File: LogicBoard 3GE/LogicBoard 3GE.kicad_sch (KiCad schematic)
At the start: 163 parts, among them IC201 2363, IC202 74LS00, IC203 74LS32, IC204 2114, IC205 2114, IC206 68A09, IC207 6522, IC208 AY3-8912, IC301 MC1408, IC302 CD4052B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

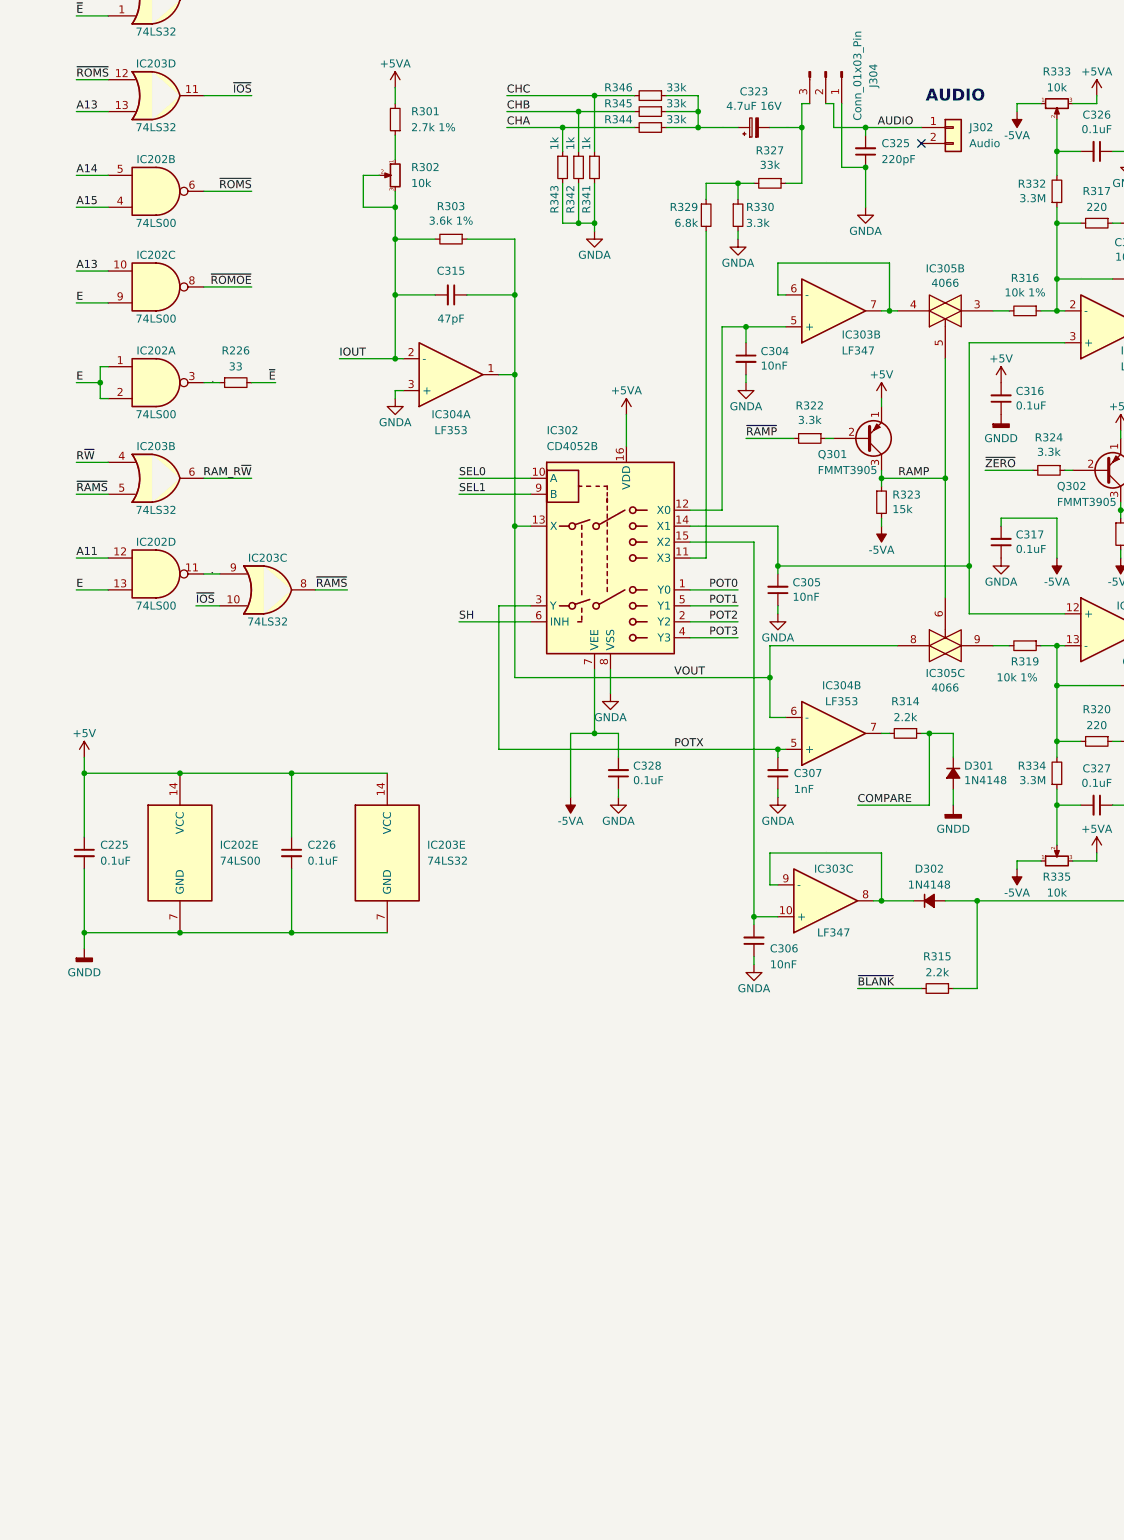
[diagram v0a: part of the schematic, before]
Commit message: added lm386 audio circuit
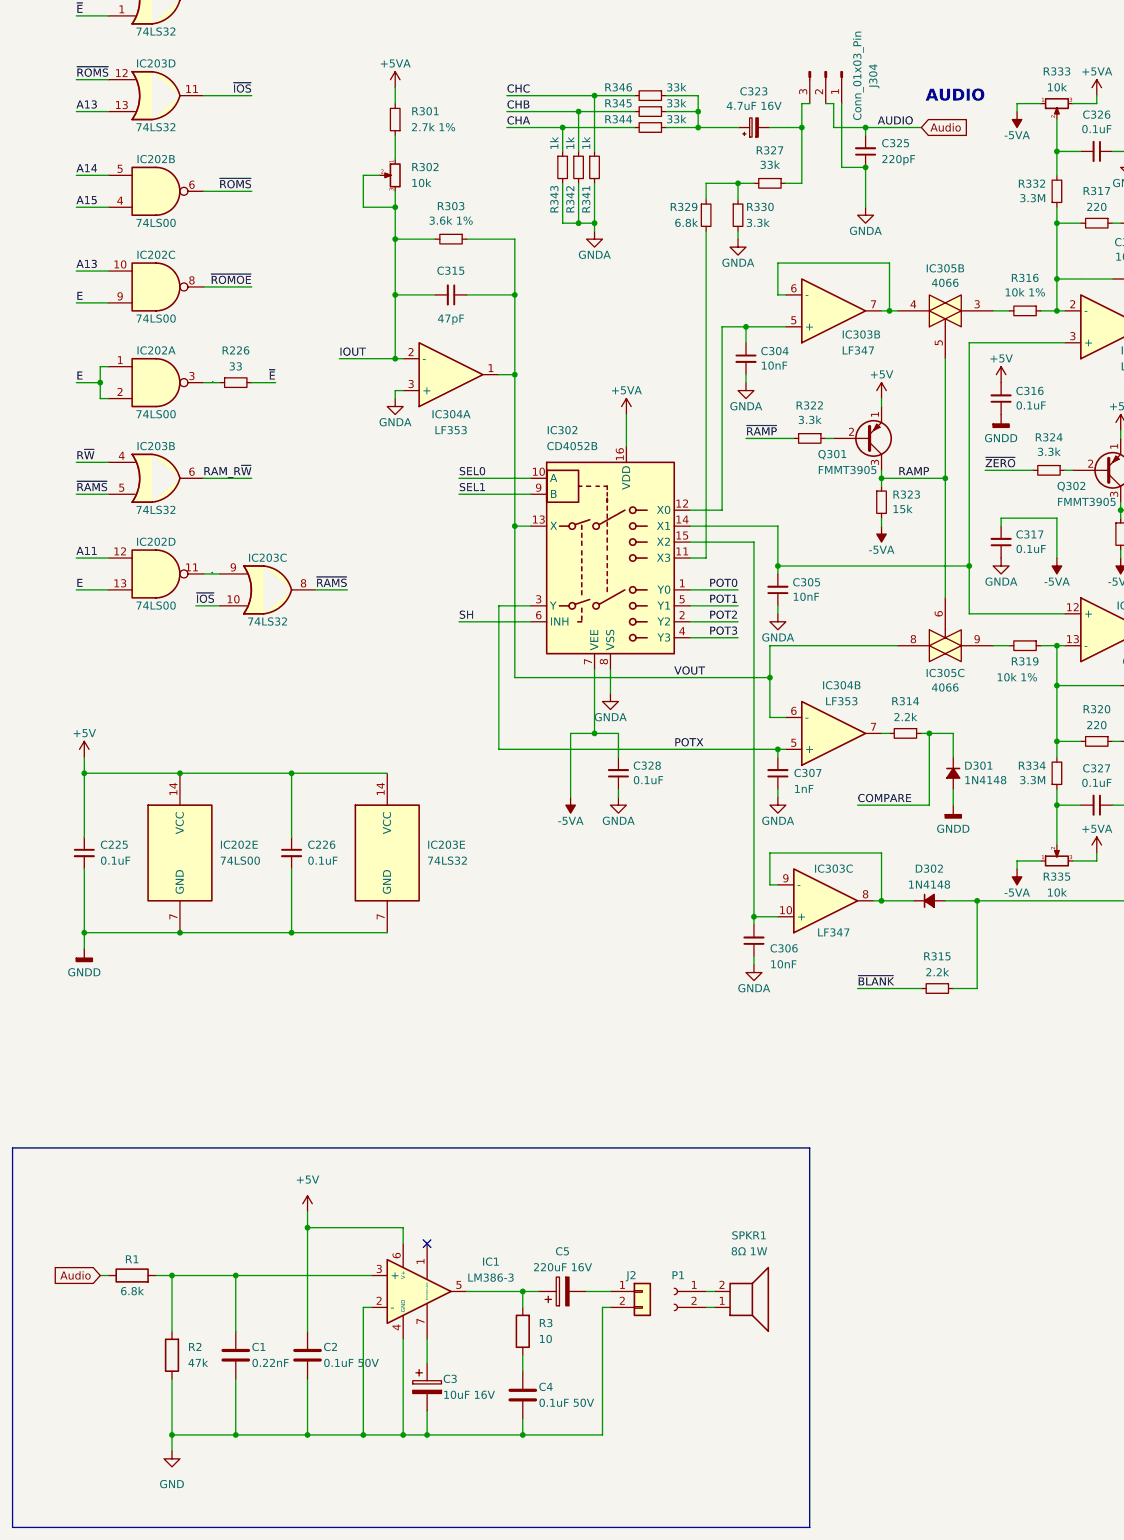
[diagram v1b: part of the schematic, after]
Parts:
- removed J302: Audio, Connector_Molex:Molex_KK-254_AE-6410-02A_1x02_P2.54mm_Vertical, symbol Connector_Generic:Conn_01x02
- added C1: 0.22nF, symbol Device:C
- added C2, C4: 0.1uF 50V, symbol Device:C
- added C3: 10uF 16V, symbol Device:C_Polarized
- added C5: 220uF 16V, symbol Device:C_Polarized
- added IC1: LM386-3, symbol Vectrex:LM386-3
- added J2: Conn_01x02, symbol Connector_Generic:Conn_01x02
- added P1: Conn_01x02_Female, symbol Connector:Conn_01x02_Female
- added R1: 6.8k, symbol Device:R
- added R2: 47k, symbol Device:R
- added R3: 10, symbol Device:R
- added SPKR1: 8Ω 1W, symbol Device:Speaker
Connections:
- net +5V: now also C2.2, IC1.6 (V+)
- net GND: now also C1.2, C2.1, C3.2, C4.2, IC1.2 (-), IC1.4 (GND), J2.2 (Pin_2), R2.1
- net AUDIO renamed Audio
- net Audio: now also R1.1
- new net: P1.2 (Pin_2), SPKR1.1
- new net: P1.1 (Pin_1), SPKR1.2
- new net: C4.1, R3.1
- new net: C5.1, IC1.5, R3.2
- new net: C1.1, IC1.3 (+), R1.2, R2.2
- new net: C3.1, IC1.7 (BYPASS)
- new net: C5.2, J2.1 (Pin_1)

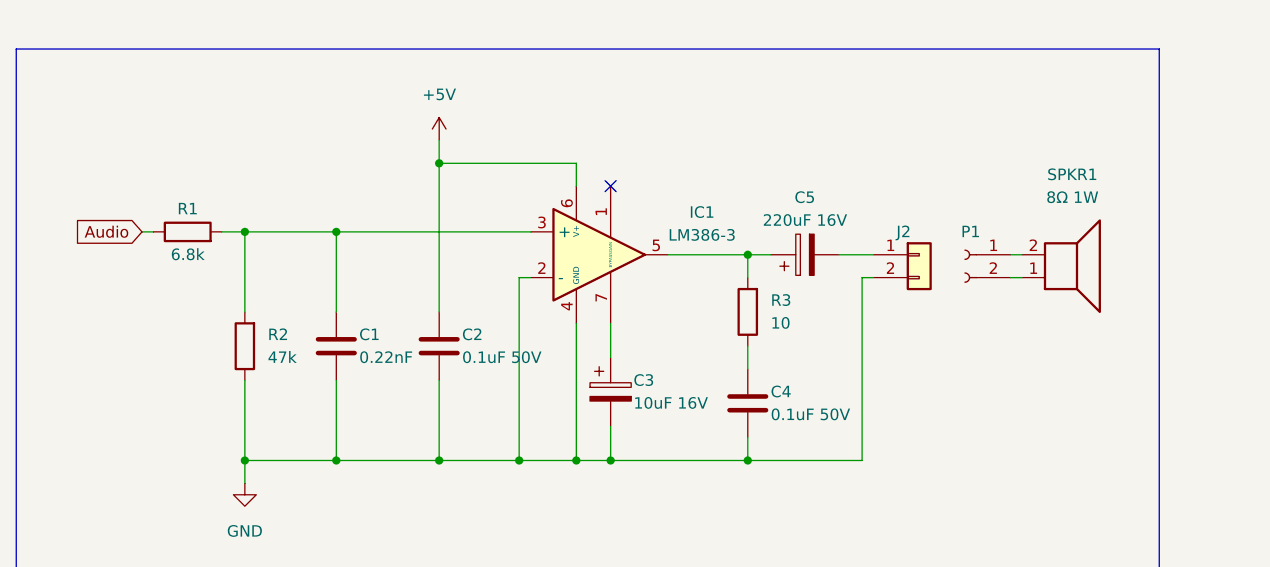
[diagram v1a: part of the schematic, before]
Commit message: added lm386 again, Added MD_90SM footprint. Solve all DRC Conflicts
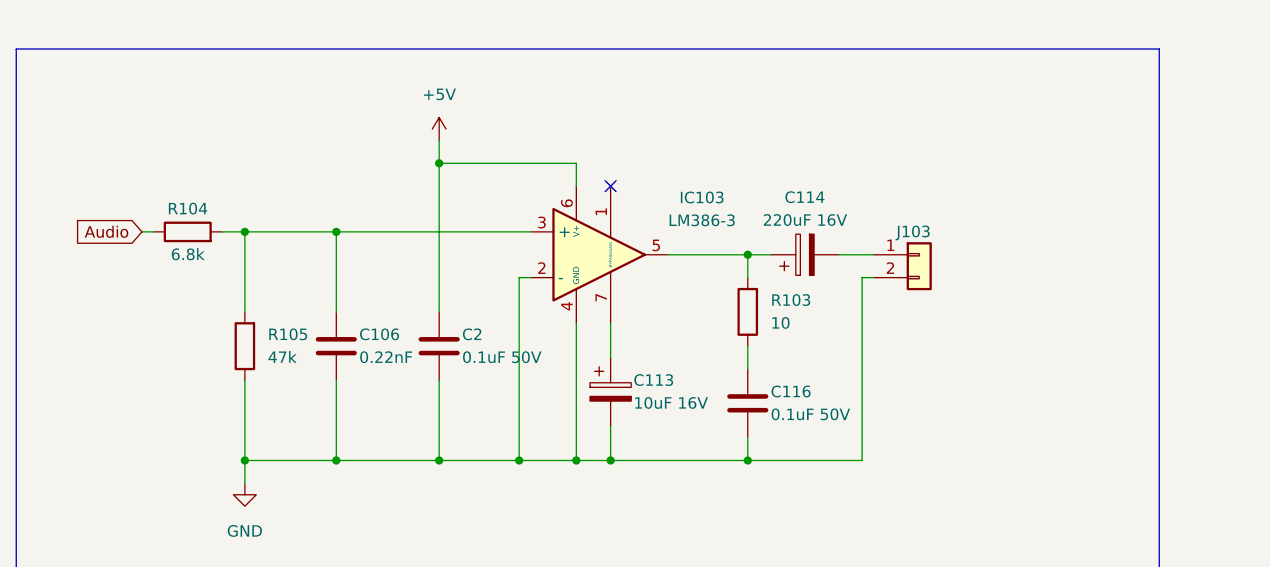
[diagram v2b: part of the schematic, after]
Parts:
- removed P1: Conn_01x02_Female, symbol Connector:Conn_01x02_Female
- removed SPKR1: 8Ω 1W, symbol Device:Speaker
- C106: renamed from C1; footprint (none) -> Capacitor_SMD:C_0805_2012Metric
- C113: renamed from C3; footprint (none) -> Capacitor_SMD:CP_Elec_4x5.3
- C114: renamed from C5; footprint (none) -> Capacitor_SMD:CP_Elec_8x10.5
- C116: renamed from C4; footprint (none) -> Capacitor_SMD:C_0805_2012Metric
- C2: footprint (none) -> Capacitor_SMD:C_0805_2012Metric
- IC103: renamed from IC1; footprint (none) -> Package_SO:SOIC-8-1EP_3.9x4.9mm_P1.27mm_EP2.29x3mm
- J103: renamed from J2; footprint (none) -> Connector_JST:JST_EH_B2B-EH-A_1x02_P2.50mm_Vertical
- R103: renamed from R3; footprint (none) -> Resistor_SMD:R_0805_2012Metric
- R104: renamed from R1; footprint (none) -> Resistor_SMD:R_0805_2012Metric
- R105: renamed from R2; footprint (none) -> Resistor_SMD:R_0805_2012Metric
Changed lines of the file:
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@@
 	(wire
 		(pts
-			(xy 125.73 326.39) (xy 127 326.39)
-		)
-		(stroke
-			(width 0)
-			(type default)
-		)
-	)
-	(wire
-		(pts
 			(xy 255.27 245.11) (xy 275.59 245.11)
 		)
@@
 	(wire
 		(pts
-			(xy 125.73 323.85) (xy 127 323.85)
-		)
-		(stroke
-			(width 0)
-			(type default)
-		)
-	)
-	(wire
-		(pts
 			(xy 153.67 200.66) (xy 153.67 201.93)
 		)
@@
 	)
 	(symbol
-		(lib_id "Device:Speaker")
-		(at 132.08 326.39 0)
-		(mirror x)
-		(unit 1)
-		(exclude_from_sim no)
-		(in_bom yes)
-		(on_board yes)
-		(dnp no)
-		(fields_autoplaced yes)
-		(property "Reference" "SPKR1"
-			(at 132.588 314.96 0)
-			(effects
-				(font
-					(size 1.27 1.27)
-				)
-			)
-		)
-		(property "Value" "8Ω 1W"
-			(at 132.588 317.5 0)
-			(effects
-				(font
-					(size 1.27 1.27)
-				)
-			)
-		)
-		(property "Footprint" ""
-			(at 132.08 321.31 0)
-			(effects
-				(font
-					(size 1.27 1.27)
-				)
-				(hide yes)
-			)
-		)
-		(property "Datasheet" "~"
-			(at 131.826 325.12 0)
-			(effects
-				(font
-					(size 1.27 1.27)
-				)
-				(hide yes)
-			)
-		)
-		(property "Description" ""
-			(at 132.08 326.39 0)
-			(effects
-				(font
-					(size 1.27 1.27)
-				)
-				(hide yes)
-			)
-		)
-		(pin "1"
-		)
-		(pin "2"
-		)
-		(instances
-			(project "LogicBoard 3GE"
-				(path "/e63e39d7-6ac0-4ffd-8aa3-1841a4541b55"
-					(reference "SPKR1")
-					(unit 1)
-				)
-			)
-		)
-	)
-	(symbol
 		(lib_id "Device:C_Small")
 		(at 194.31 227.33 270)
@@
 		(dnp no)
 		(fields_autoplaced yes)
-		(property "Reference" "R3"
+		(property "Reference" "R103"
 			(at 99.06 328.9299 0)
 			(effects
@@
 			)
 		)
-		(property "Footprint" ""
+		(property "Footprint" "Resistor_SMD:R_0805_2012Metric"
 			(at 98.298 330.2 90)
 			(effects
@@
 			(project "LogicBoard 3GE"
 				(path "/e63e39d7-6ac0-4ffd-8aa3-1841a4541b55"
-					(reference "R3")
+					(reference "R103")
 					(unit 1)
 				)
@@
 			)
 		)
-		(property "Footprint" ""
+		(property "Footprint" "Capacitor_SMD:C_0805_2012Metric"
 			(at 61.2648 330.2 0)
 			(effects
@@
 	)
 	(symbol
-		(lib_id "Connector:Conn_01x02_Female")
-		(at 120.65 323.85 0)
-		(mirror y)
-		(unit 1)
-		(exclude_from_sim no)
-		(in_bom yes)
-		(on_board yes)
-		(dnp no)
-		(fields_autoplaced yes)
-		(property "Reference" "P1"
-			(at 121.285 321.31 0)
-			(effects
-				(font
-					(size 1.27 1.27)
-				)
-			)
-		)
-		(property "Value" "Conn_01x02_Female"
-			(at 121.285 328.93 0)
-			(effects
-				(font
-					(size 1.27 1.27)
-				)
-				(hide yes)
-			)
-		)
-		(property "Footprint" ""
-			(at 120.65 323.85 0)
-			(effects
-				(font
-					(size 1.27 1.27)
-				)
-				(hide yes)
-			)
-		)
-		(property "Datasheet" "~"
-			(at 120.65 323.85 0)
-			(effects
-				(font
-					(size 1.27 1.27)
-				)
-				(hide yes)
-			)
-		)
-		(property "Description" ""
-			(at 120.65 323.85 0)
-			(effects
-				(font
-					(size 1.27 1.27)
-				)
-				(hide yes)
-			)
-		)
-		(pin "1"
-		)
-		(pin "2"
-		)
-		(instances
-			(project "LogicBoard 3GE"
-				(path "/e63e39d7-6ac0-4ffd-8aa3-1841a4541b55"
-					(reference "P1")
-					(unit 1)
-				)
-			)
-		)
-	)
-	(symbol
 		(lib_id "Mechanical:MountingHole_Pad")
 		(at 257.81 264.16 0)
@@
 		(on_board yes)
 		(dnp no)
-		(property "Reference" "R1"
+		(property "Reference" "R104"
 			(at 34.29 318.77 90)
 			(effects
@@
 			)
 		)
-		(property "Footprint" ""
+		(property "Footprint" "Resistor_SMD:R_0805_2012Metric"
 			(at 34.29 323.088 90)
 			(effects
@@
 			(project "LogicBoard 3GE"
 				(path "/e63e39d7-6ac0-4ffd-8aa3-1841a4541b55"
-					(reference "R1")
+					(reference "R104")
 					(unit 1)
 				)
@@
 		(on_board yes)
 		(dnp no)
-		(property "Reference" "R2"
+		(property "Reference" "R105"
 			(at 43.18 332.74 0)
 			(effects
@@
 			)
 		)
-		(property "Footprint" ""
+		(property "Footprint" "Resistor_SMD:R_0805_2012Metric"
 			(at 42.418 334.01 90)
 			(effects
@@
 			(project "LogicBoard 3GE"
 				(path "/e63e39d7-6ac0-4ffd-8aa3-1841a4541b55"
-					(reference "R2")
+					(reference "R105")
 					(unit 1)
 				)
@@
 		(on_board yes)
 		(dnp no)
-		(property "Reference" "C3"
+		(property "Reference" "C113"
 			(at 83.82 337.82 0)
 			(effects
@@
 			)
 		)
-		(property "Footprint" ""
+		(property "Footprint" "Capacitor_SMD:CP_Elec_4x5.3"
 			(at 82.2452 342.9 0)
 			(effects
@@
 			(project "LogicBoard 3GE"
 				(path "/e63e39d7-6ac0-4ffd-8aa3-1841a4541b55"
-					(reference "C3")
+					(reference "C113")
 					(unit 1)
 				)
@@
 		(on_board yes)
 		(dnp no)
-		(property "Reference" "J2"
+		(property "Reference" "J103"
 			(at 113.03 321.31 0)
 			(effects
@@
 			)
 		)
-		(property "Footprint" ""
+		(property "Footprint" "Connector_JST:JST_EH_B2B-EH-A_1x02_P2.50mm_Vertical"
 			(at 115.57 323.85 0)
 			(effects
@@
 			(project "LogicBoard 3GE"
 				(path "/e63e39d7-6ac0-4ffd-8aa3-1841a4541b55"
-					(reference "J2")
+					(reference "J103")
 					(unit 1)
 				)
@@
 		(on_board yes)
 		(dnp no)
-		(property "Reference" "C5"
+		(property "Reference" "C114"
 			(at 102.87 317.5 90)
 			(effects
@@
 			)
 		)
-		(property "Footprint" ""
+		(property "Footprint" "Capacitor_SMD:CP_Elec_8x10.5"
 			(at 106.68 322.8848 0)
 			(effects
@@
 			(project "LogicBoard 3GE"
 				(path "/e63e39d7-6ac0-4ffd-8aa3-1841a4541b55"
-					(reference "C5")
+					(reference "C114")
 					(unit 1)
 				)
@@
 		(on_board yes)
 		(dnp no)
-		(property "Reference" "C1"
+		(property "Reference" "C106"
 			(at 53.34 332.74 0)
 			(effects
@@
 			)
 		)
-		(property "Footprint" ""
+		(property "Footprint" "Capacitor_SMD:C_0805_2012Metric"
 			(at 51.7652 337.82 0)
 			(effects
@@
 			(project "LogicBoard 3GE"
 				(path "/e63e39d7-6ac0-4ffd-8aa3-1841a4541b55"
-					(reference "C1")
+					(reference "C106")
 					(unit 1)
 				)
@@
 		(on_board yes)
 		(dnp no)
-		(property "Reference" "C4"
+		(property "Reference" "C116"
 			(at 99.06 339.09 0)
 			(effects
@@
 			)
 		)
-		(property "Footprint" ""
+		(property "Footprint" "Capacitor_SMD:C_0805_2012Metric"
 			(at 97.4852 344.17 0)
 			(effects
@@
 			(project "LogicBoard 3GE"
 				(path "/e63e39d7-6ac0-4ffd-8aa3-1841a4541b55"
-					(reference "C4")
+					(reference "C116")
 					(unit 1)
 				)
@@
 		(dnp no)
 		(fields_autoplaced yes)
-		(property "Reference" "IC1"
-			(at 91.44 319.151 0)
+		(property "Reference" "IC103"
+			(at 91.44 317.5314 0)
 			(effects
 				(font
@@
 		)
 		(property "Value" "LM386-3"
-			(at 91.44 321.691 0)
+			(at 91.44 320.0714 0)
 			(effects
 				(font
@@
 			)
 		)
-		(property "Footprint" ""
+		(property "Footprint" "Package_SO:SOIC-8-1EP_3.9x4.9mm_P1.27mm_EP2.29x3mm"
 			(at 78.232 342.646 0)
 			(effects
@@
 			(project "LogicBoard 3GE"
 				(path "/e63e39d7-6ac0-4ffd-8aa3-1841a4541b55"
-					(reference "IC1")
+					(reference "IC103")
 					(unit 1)
 				)

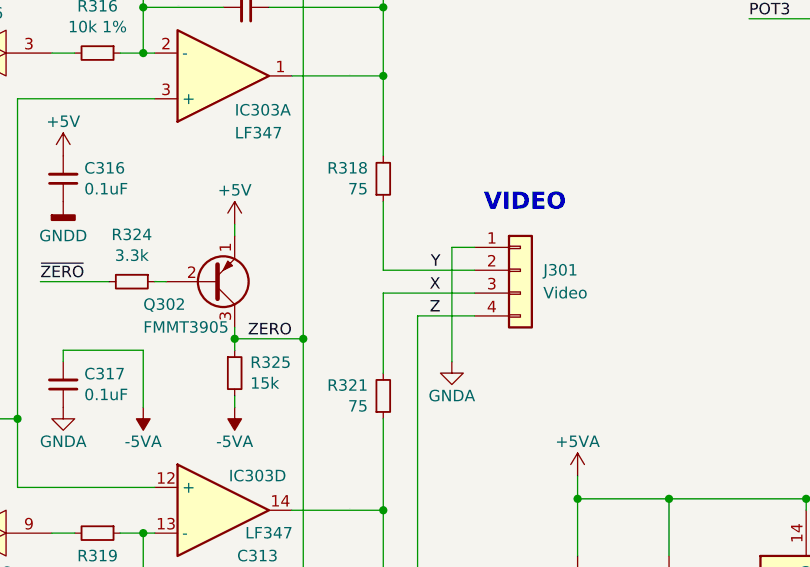
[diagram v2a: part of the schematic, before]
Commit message: resolve DRC violations, various shorts to +5V
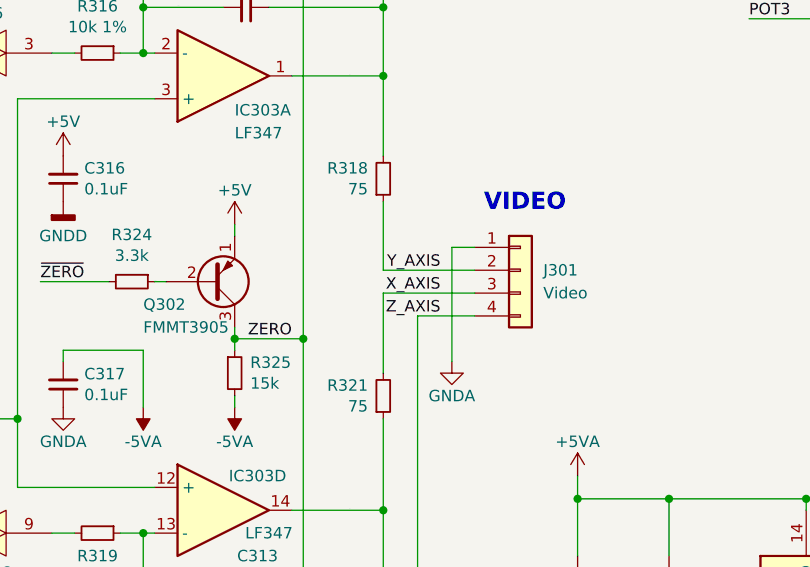
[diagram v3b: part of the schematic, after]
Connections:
- net X renamed X_AXIS
- net Y renamed Y_AXIS
- net Z renamed Z_AXIS
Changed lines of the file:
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@@
 		)
 	)
-	(label "Y"
+	(label "Y_AXIS"
 		(at 214.63 191.77 180)
 		(fields_autoplaced yes)
@@
 		)
 	)
-	(label "X"
+	(label "X_AXIS"
 		(at 214.63 194.31 180)
 		(fields_autoplaced yes)
@@
 		)
 	)
-	(label "Z"
+	(label "Z_AXIS"
 		(at 214.63 196.85 180)
 		(fields_autoplaced yes)
